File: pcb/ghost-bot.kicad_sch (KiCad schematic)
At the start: 35 parts, among them J1 Conn_01x03_Pin, J2 Conn_01x03_Pin, J3 Conn_01x04_Pin, J4 Conn_01x02_Pin, SW1 SW_Push, SW2 SW_Push, SW3 Switch

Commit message: Replace battery connector with footprints that include strain relief, change rgb led footprint
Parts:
- J4: footprint Connector_PinHeader_2.54mm:PinHeader_1x02_P2.54mm_Vertical -> Connector_Wire:SolderWire-0.1sqmm_1x02_P3.6mm_D0.4mm_OD1mm_Relief
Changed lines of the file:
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@@
 			)
 		)
-		(property "Footprint" "Connector_PinHeader_2.54mm:PinHeader_1x02_P2.54mm_Vertical"
+		(property "Footprint" "Connector_Wire:SolderWire-0.1sqmm_1x02_P3.6mm_D0.4mm_OD1mm_Relief"
 			(at 134.62 49.53 0)
 			(effects

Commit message: Add missing save in the schematic (footprint change)
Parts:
- D1: footprint LED_THT:LED_D5.0mm-4_RGB -> LED_THT:LED_D5.0mm-4_RGB_Staggered_Pins
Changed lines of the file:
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@@
 			)
 		)
-		(property "Footprint" "LED_THT:LED_D5.0mm-4_RGB"
+		(property "Footprint" "LED_THT:LED_D5.0mm-4_RGB_Staggered_Pins"
 			(at 76.2 135.89 0)
 			(effects

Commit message: Minor silkscreen changes before generating gerbers/drill
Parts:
- D1: Mfr Part Number (none) -> L-154A4SURKQBDZGW; Supplier (none) -> Element 14; Supplier Part Number (none) -> 2290374
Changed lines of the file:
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@@
+			)
+		)
+		(property "Mfr Part Number" " L-154A4SURKQBDZGW"
+			(at 76.2 134.62 0)
+			(effects
+				(font
+					(size 1.27 1.27)
+				)
+				(hide yes)
+			)
+		)
+		(property "Supplier" "Element 14"
+			(at 76.2 134.62 0)
+			(effects
+				(font
+					(size 1.27 1.27)
+				)
+				(hide yes)
+			)
+		)
+		(property "Supplier Part Number" " 2290374"
+			(at 76.2 134.62 0)
+			(effects
+				(font
+					(size 1.27 1.27)
+				)
+				(hide yes)
 			)
 		)

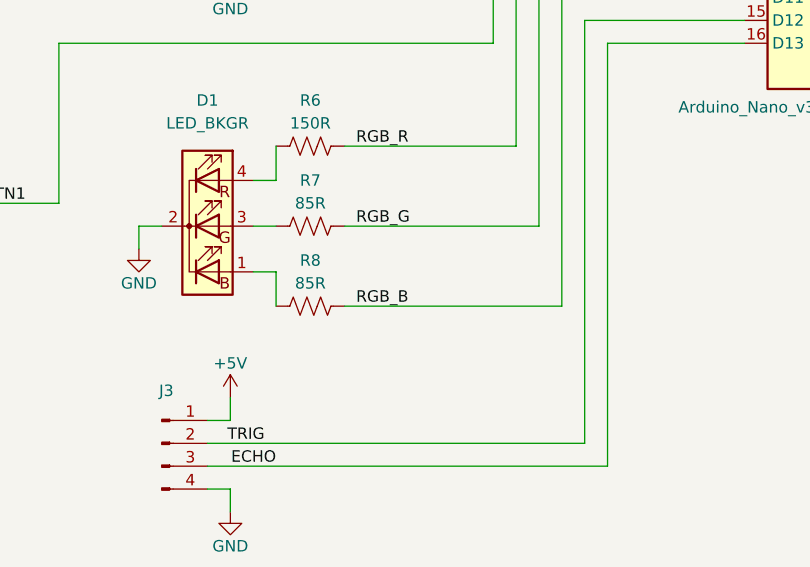
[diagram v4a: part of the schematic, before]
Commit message: Add part numbers to schematic, remove csv from gitignore, generate csv bom
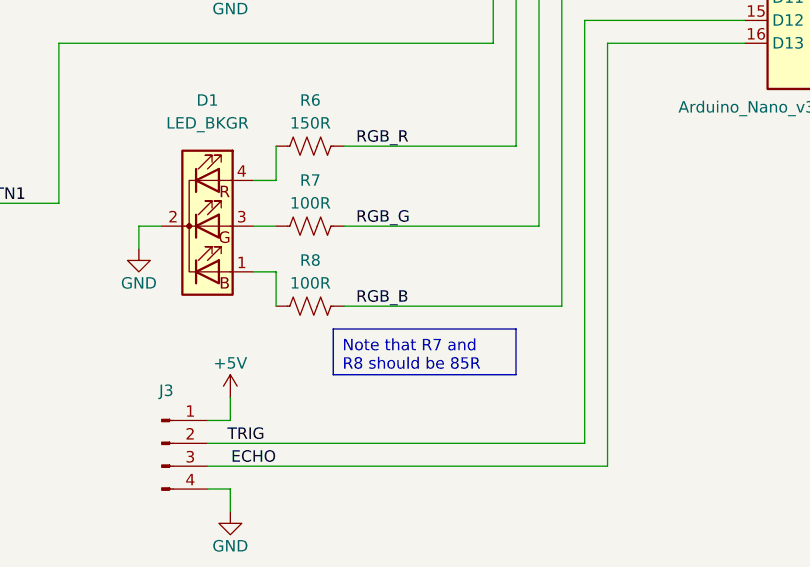
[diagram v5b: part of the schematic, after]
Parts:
- A1: Manufacturer Part Number (none) -> A000005; Supplier  (none) -> Element 14; Supplier Part Number (none) -> 1848691
- BT1: Manufacturer Part Number (none) -> 2478; Supplier  (none) -> Element 14; Supplier Part Number (none) -> 1650685
- D1: Manufacturer Part Number (none) -> L-154A4SURKQBDZGW; Mfr Part Number L-154A4SURKQBDZGW -> (none); Supplier Element 14 -> (none); Supplier  (none) -> Element 14
- D10, D5, D9: Manufacturer Part Number (none) -> SFH203-FA; Supplier  (none) -> Element 14; Supplier Part Number (none) -> 1212743
- D2, D3, D4: Manufacturer Part Number (none) -> MCL053GD; Supplier  (none) -> Element 14; Supplier Part Number (none) -> 1581138
- D6, D7, D8: Manufacturer Part Number (none) -> OFL-5102; Supplier  (none) -> Element 14; Supplier Part Number (none) -> 1716710
- J1, J2: Manufacturer Part Number (none) -> 2211S-03G; Supplier  (none) -> Element 14; Supplier Part Number (none) -> 1593412
- J3: Manufacturer Part Number (none) -> 2211S-04G; Supplier  (none) -> Element 14; Supplier Part Number (none) -> 1593413
- J4: Manufacturer Part Number (none) -> NA; Supplier  (none) -> NA; Supplier Part Number (none) -> NA
- R1, R2: Manufacturer Part Number (none) -> MCF 0.25W 10K; Supplier  (none) -> Element 14; Supplier Part Number (none) -> 9339060
- R10, R11, R12: Manufacturer Part Number (none) -> MCF 0.25W 100R; Supplier  (none) -> Element 14; Supplier Part Number (none) -> 9339043
- R13, R14, R9: Manufacturer Part Number (none) -> MCF 0.25W 100K; Supplier  (none) -> Element 14; Supplier Part Number (none) -> 9339078
- R3, R4, R5: Manufacturer Part Number (none) -> MCF 0.25W 330R; Supplier  (none) -> Element 14; Supplier Part Number (none) -> 9339418
- R6: Manufacturer Part Number (none) -> MCF 0.25W 150R; Supplier  (none) -> Element 14; Supplier Part Number (none) -> 9339175
- R7, R8: value 85R -> 100R; Manufacturer Part Number (none) -> MCF 0.25W 100R; Supplier  (none) -> Element 14; Supplier Part Number (none) -> 9339043
- SW1, SW2: Manufacturer Part Number (none) -> 1825910-6; Supplier  (none) -> Element 14; Supplier Part Number (none) -> 2456210
- SW3: Manufacturer Part Number (none) -> EG1271; Supplier  (none) -> Element 14; Supplier Part Number (none) -> 4050998
- U1, U2: Manufacturer Part Number (none) -> MP-708-0002; Supplier  (none) -> Element 14; Supplier Part Number (none) -> 3359812

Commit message: Update 330 and 100k resistor part numbers for parts that are available now
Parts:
- R13, R14, R9: Manufacturer Part Number MCF 0.25W 100K -> MF25 100K; Supplier Part Number 9339078 -> 9341129
- R3, R4, R5: Manufacturer Part Number MCF 0.25W 330R -> MF25 330R; Supplier Part Number 9339418 -> 9341730
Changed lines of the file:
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@@
 			)
 		)
-		(property "Manufacturer Part Number" "MCF 0.25W 330R"
+		(property "Manufacturer Part Number" "MF25 330R"
 			(at 71.12 57.15 90)
 			(effects
@@
 			)
 		)
-		(property "Supplier Part Number" "9339418"
+		(property "Supplier Part Number" "9341730"
 			(at 71.12 57.15 90)
 			(effects
@@
 			)
 		)
-		(property "Manufacturer Part Number" "MCF 0.25W 100K"
+		(property "Manufacturer Part Number" "MF25 100K"
 			(at 228.6 102.87 0)
 			(effects
@@
 			)
 		)
-		(property "Supplier Part Number" "9339078"
+		(property "Supplier Part Number" "9341129"
 			(at 228.6 102.87 0)
 			(effects
@@
 			)
 		)
-		(property "Manufacturer Part Number" "MCF 0.25W 100K"
+		(property "Manufacturer Part Number" "MF25 100K"
 			(at 210.82 102.87 0)
 			(effects
@@
 			)
 		)
-		(property "Supplier Part Number" "9339078"
+		(property "Supplier Part Number" "9341129"
 			(at 210.82 102.87 0)
 			(effects
@@
 			)
 		)
-		(property "Manufacturer Part Number" "MCF 0.25W 330R"
+		(property "Manufacturer Part Number" "MF25 330R"
 			(at 71.12 46.99 90)
 			(effects
@@
 			)
 		)
-		(property "Supplier Part Number" "9339418"
+		(property "Supplier Part Number" "9341730"
 			(at 71.12 46.99 90)
 			(effects
@@
 			)
 		)
-		(property "Manufacturer Part Number" "MCF 0.25W 330R"
+		(property "Manufacturer Part Number" "MF25 330R"
 			(at 71.12 68.58 90)
 			(effects
@@
 			)
 		)
-		(property "Supplier Part Number" "9339418"
+		(property "Supplier Part Number" "9341730"
 			(at 71.12 68.58 90)
 			(effects
@@
 			)
 		)
-		(property "Manufacturer Part Number" "MCF 0.25W 100K"
+		(property "Manufacturer Part Number" "MF25 100K"
 			(at 247.65 102.87 0)
 			(effects
@@
 			)
 		)
-		(property "Supplier Part Number" "9339078"
+		(property "Supplier Part Number" "9341129"
 			(at 247.65 102.87 0)
 			(effects

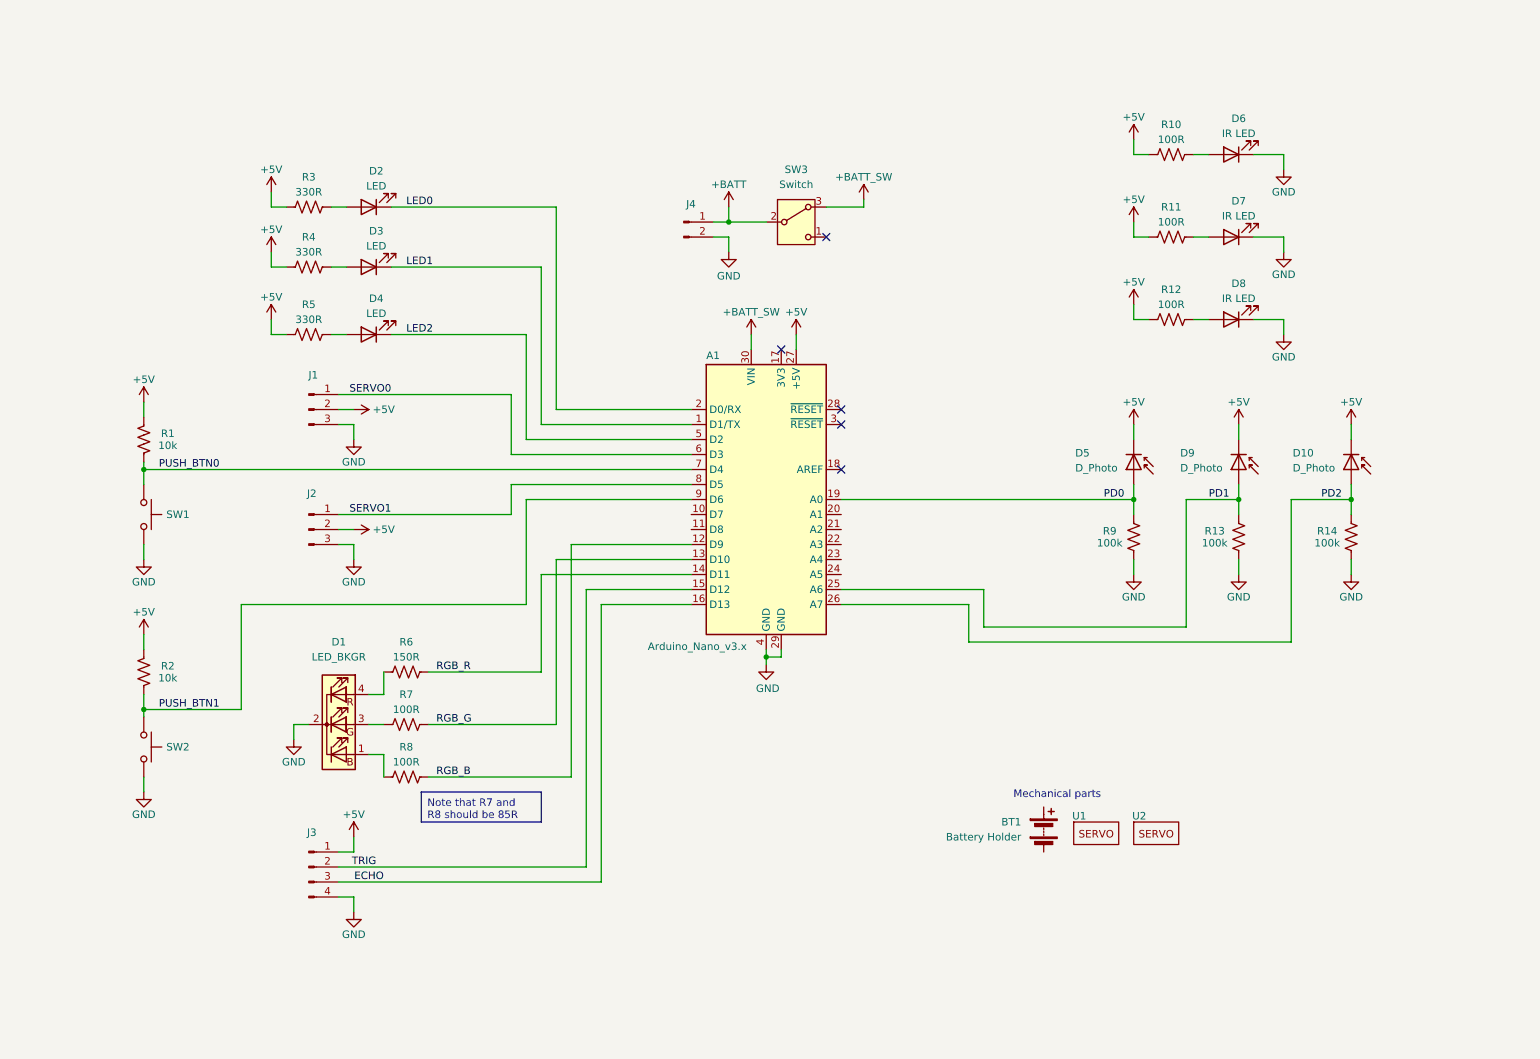
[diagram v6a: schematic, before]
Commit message: Issue-6: Move LEDs, breakout unused pins
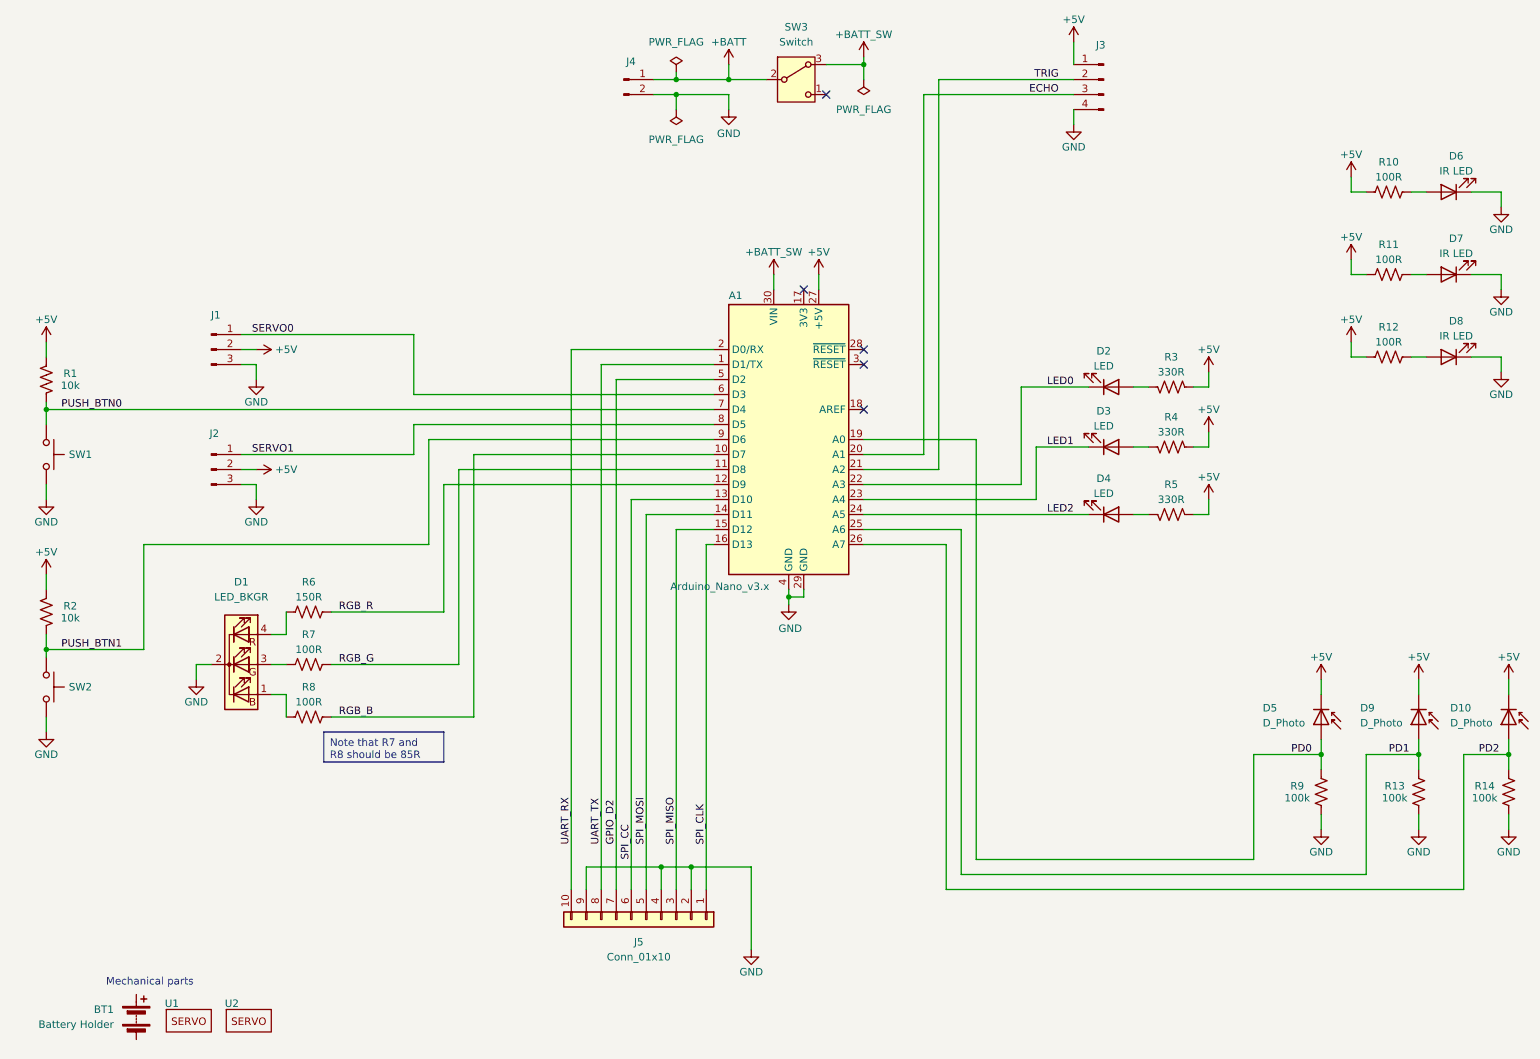
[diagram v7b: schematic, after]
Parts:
- added J5: Conn_01x10, Connector_PinSocket_2.54mm:PinSocket_1x10_P2.54mm_Vertical, symbol Connector_Generic:Conn_01x10
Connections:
- net ECHO: now also A1.20 (A1); no longer A1.16 (D13)
- net GND: now also J5.2 (Pin_2), J5.4 (Pin_4), J5.9 (Pin_9)
- net LED0: now also A1.22 (A3); no longer A1.2 (D0/RX)
- net LED1: now also A1.23 (A4); no longer A1.1 (D1/TX)
- net LED2: now also A1.24 (A5); no longer A1.5 (D2)
- net RGB_B: now also A1.10 (D7); no longer A1.12 (D9)
- net RGB_G: now also A1.11 (D8); no longer A1.13 (D10)
- net RGB_R: now also A1.12 (D9); no longer A1.14 (D11)
- net TRIG: now also A1.21 (A2); no longer A1.15 (D12)
- new net GPIO_D2: A1.5 (D2), J5.7 (Pin_7)
- new net SPI_CC: A1.13 (D10), J5.6 (Pin_6)
- new net SPI_CLK: A1.16 (D13), J5.1 (Pin_1)
- new net SPI_MISO: A1.15 (D12), J5.3 (Pin_3)
- new net SPI_MOSI: A1.14 (D11), J5.5 (Pin_5)
- new net UART_RX: A1.2 (D0/RX), J5.10 (Pin_10)
- new net UART_TX: A1.1 (D1/TX), J5.8 (Pin_8)
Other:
- moved on the sheet: A1, BT1, D1, D10, D2, D3, D4, D5, D6, D7, D8, D9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

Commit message: Separate UART and SPI connectors, reroute tracks, move buttons
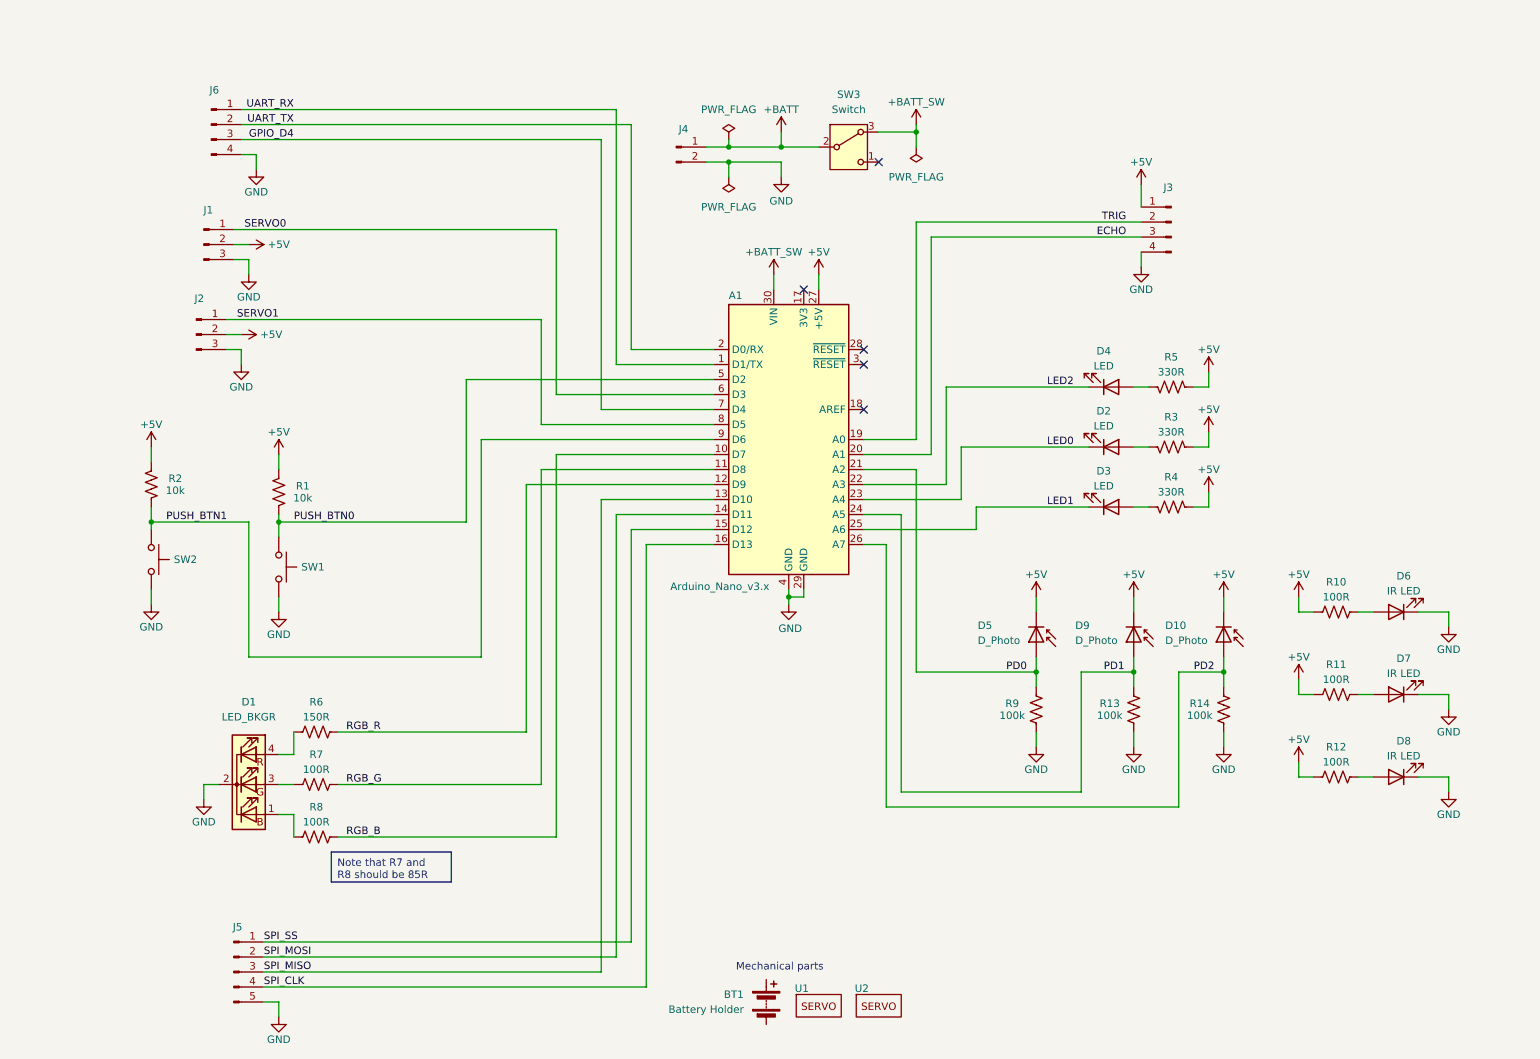
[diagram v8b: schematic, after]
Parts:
- removed J5: Conn_01x10, Connector_PinSocket_2.54mm:PinSocket_1x10_P2.54mm_Vertical, symbol Connector_Generic:Conn_01x10
- added J5: Conn_01x05_Pin, Connector_PinHeader_2.54mm:PinHeader_1x05_P2.54mm_Vertical, symbol Connector:Conn_01x05_Pin
- added J6: Conn_01x04_Pin, Connector_PinHeader_2.54mm:PinHeader_1x04_P2.54mm_Vertical, symbol Connector:Conn_01x04_Pin
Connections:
- net GPIO_D2 is gone; now on net PUSH_BTN0: A1.5 (D2)
- net SPI_CC is gone; now on net SPI_MISO: A1.13 (D10)
- net GND: now also J5.5 (Pin_5), J6.4 (Pin_4)
- net LED0: now also A1.23 (A4); no longer A1.22 (A3)
- net LED1: now also A1.25 (A6); no longer A1.23 (A4)
- net LED2: now also A1.22 (A3); no longer A1.24 (A5)
- net PD0: now also A1.21 (A2); no longer A1.19 (A0)
- net PD1: now also A1.24 (A5); no longer A1.25 (A6)
- net PUSH_BTN0: no longer A1.7 (D4)
- net SPI_CLK: now also J5.4 (Pin_4)
- net SPI_MISO: now also J5.3 (Pin_3); no longer A1.15 (D12)
- net SPI_MOSI: now also J5.2 (Pin_2)
- net TRIG: now also A1.19 (A0); no longer A1.21 (A2)
- net UART_RX: now also A1.1 (D1/TX), J6.1 (Pin_1); no longer A1.2 (D0/RX)
- net UART_TX: now also A1.2 (D0/RX), J6.2 (Pin_2); no longer A1.1 (D1/TX)
- new net GPIO_D4: A1.7 (D4), J6.3 (Pin_3)
- new net SPI_SS: A1.15 (D12), J5.1 (Pin_1)
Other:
- moved on the sheet: BT1, D1, D10, D2, D3, D4, D5, D6, D7, D8, D9, J1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
